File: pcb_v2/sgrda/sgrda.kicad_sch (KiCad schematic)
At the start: 17 parts, among them J1 addr_decoder, U1 74HC238, U2 74LS138, U3 74LS04

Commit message: arquivos no note
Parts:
- removed C3: 100nF, Capacitor_THT:C_Disc_D4.7mm_W2.5mm_P5.00mm, symbol Device:C
- removed unit 7 of U3
- removed unit 2 of U3
- removed unit 6 of U3
- added C4: 100nF, Capacitor_THT:C_Disc_D4.7mm_W2.5mm_P5.00mm, symbol Device:C
- added unit 7 of U4
- added unit 3 of U4
- added unit 1 of U4
- renumbered U3 to U4
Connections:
- net +5V: now also C4.1, U4.14 (VCC)
- net GND: now also C4.2, U4.7 (GND)
- net read_zero: now also U4.4; no longer U4.10
- net wr_addr_3: now also U1.4 (~{E1}); no longer U1.6 (E3)
- net write_clock: now also U1.6 (E3); no longer U1.4 (~{E1})
- net at U2.15 (O0): now also U4.3; no longer U4.11
- net enable_data_in renamed ~{enable_data_in}
- net enable_data_out renamed ~{enable_data_out}
- net n_read_A renamed ~{read_A}
- net n_read_B renamed ~{read_B}
- net n_read_C renamed ~{read_C}
- net n_read_D renamed ~{read_D}
- net n_read_E renamed ~{read_E}
- net n_read_H renamed ~{read_H}
- net n_read_L renamed ~{read_L}

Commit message: arquivos do gdrive
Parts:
- removed D1, D2, D3, D4, D5, D6: 1N4148, Diode_THT:D_DO-35_SOD27_P7.62mm_Horizontal, symbol Diode:1N4148
- removed R1, R2: 4.7K, Resistor_THT:R_Axial_DIN0207_L6.3mm_D2.5mm_P7.62mm_Horizontal, symbol Device:R
- added C3: 100nF, Capacitor_THT:C_Disc_D4.7mm_W2.5mm_P5.00mm, symbol Device:C
- added U3: 74LS32, Package_DIP:DIP-14_W7.62mm, symbol 74xx:74LS32
- D7: value LED -> POWER
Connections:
- net +5V: now also C3.1, U3.14 (VCC)
- net GND: now also U4.1, U4.11, U4.13, U4.5, U4.9, C3.2, U3.7 (GND)
- net rd_addr_3: now also U3.1
- net rd_addr_4: now also U3.2
- net read_zero: now also U3.4
- net wr_addr_3: now also U3.10
- net wr_addr_4: now also U3.9
- net write_zero: now also U3.12
- net ~{enable_data_in}: now also U3.11
- net ~{enable_data_out}: now also U3.6
- new net: U3.13, U3.8
- new net: U3.3, U3.5
- no-connect marks 23 -> 18

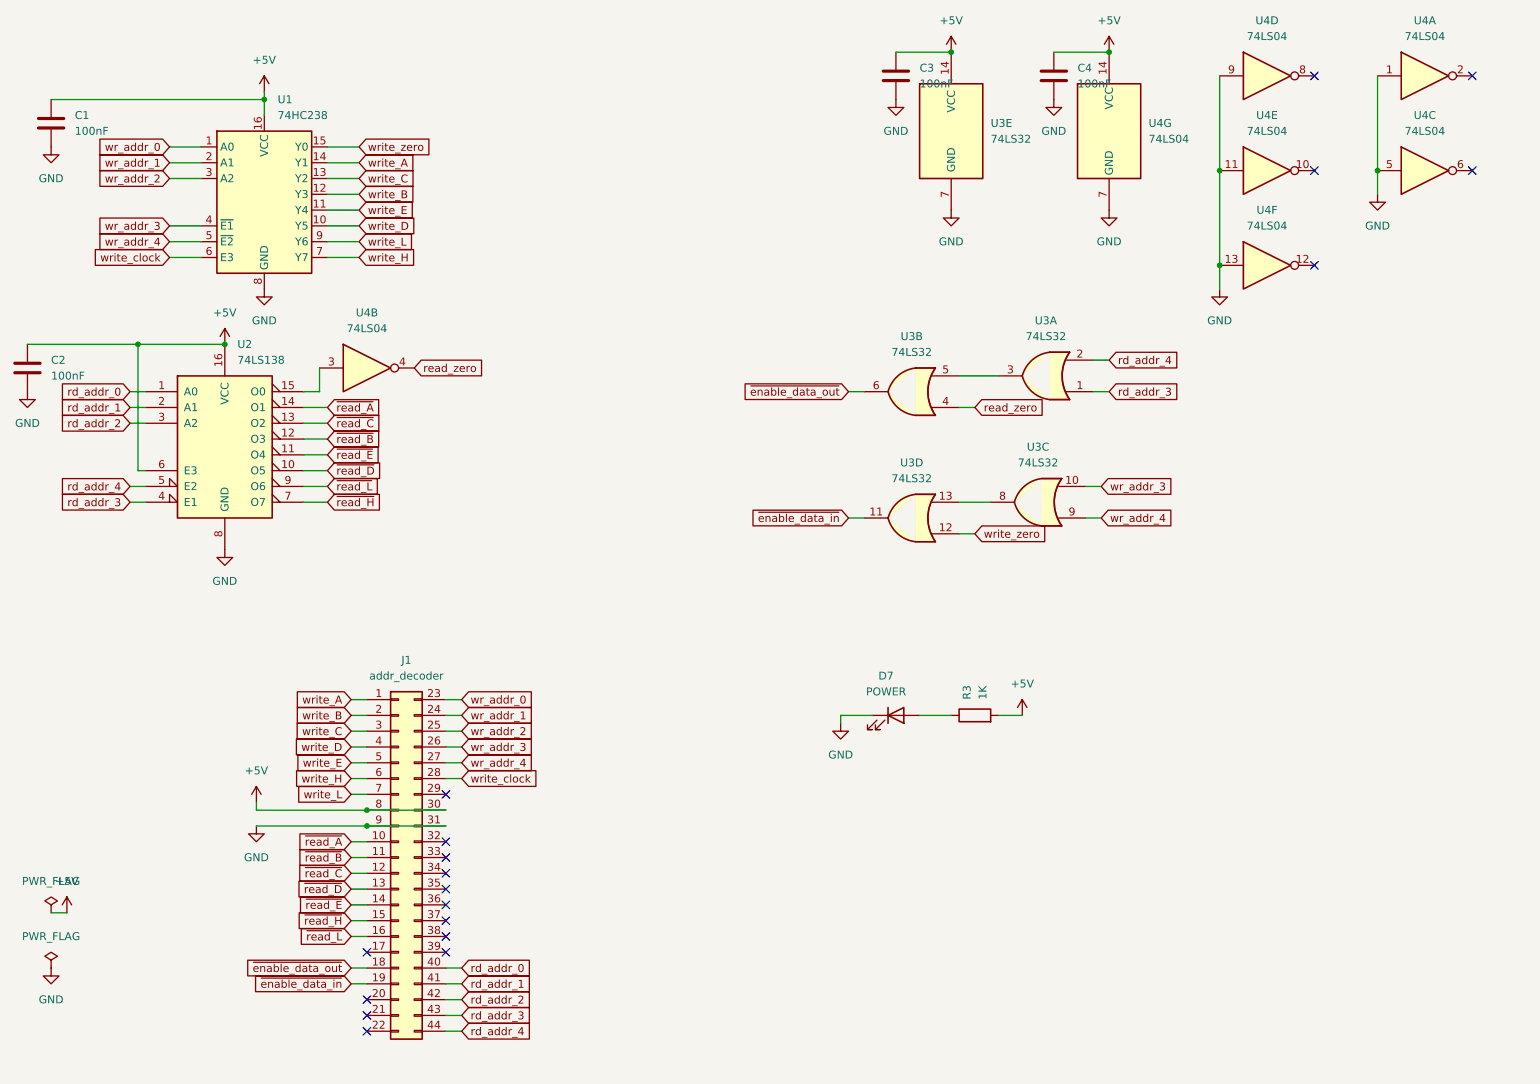
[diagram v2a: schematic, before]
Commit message: revisao completa; mgrfa agora inclui sr8 e sgrda; remover estes dois no proximo commit
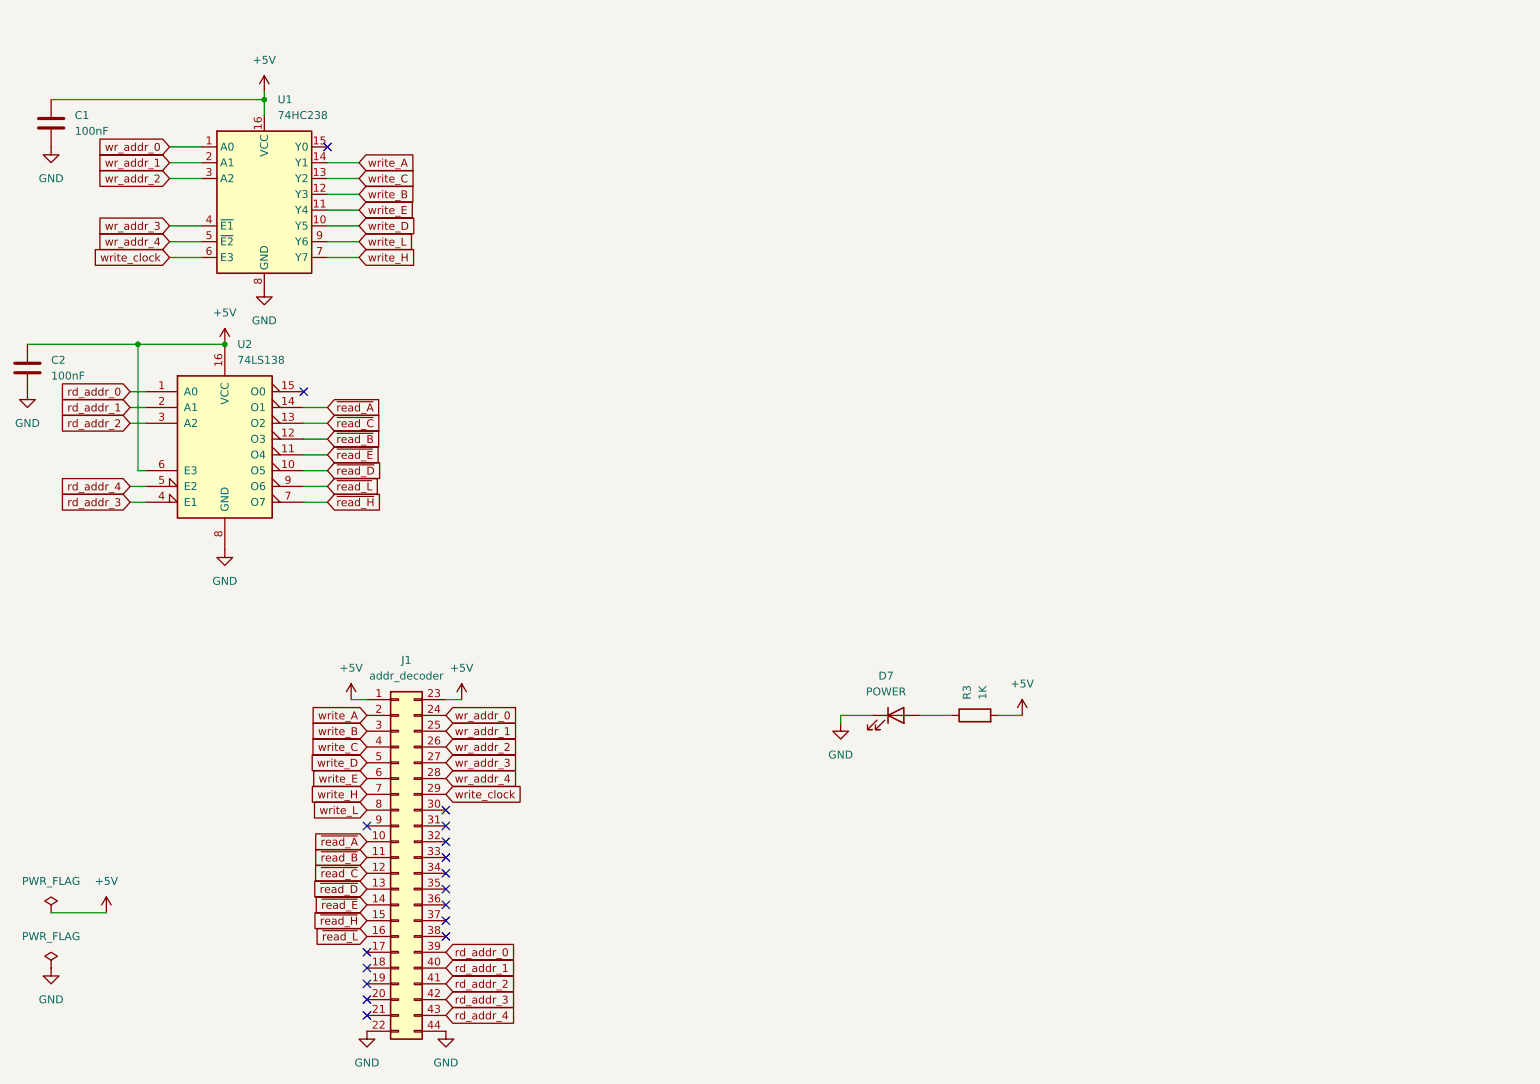
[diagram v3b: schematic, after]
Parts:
- removed C3, C4: 100nF, Capacitor_THT:C_Disc_D4.7mm_W2.5mm_P5.00mm, symbol Device:C
- removed U3: 74LS32, Package_DIP:DIP-14_W7.62mm, symbol 74xx:74LS32
- removed U4: 74LS04, Package_DIP:DIP-14_W7.62mm, symbol 74xx:74LS04
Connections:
- net +5V: now also J1.1 (Pin_1), J1.23 (Pin_23); no longer J1.30 (Pin_30), J1.8 (Pin_8)
- net GND: now also J1.22 (Pin_22), J1.44 (Pin_44); no longer J1.31 (Pin_31), J1.9 (Pin_9)
- net rd_addr_0: now also J1.39 (Pin_39); no longer J1.40 (Pin_40)
- net rd_addr_1: now also J1.40 (Pin_40); no longer J1.41 (Pin_41)
- net rd_addr_2: now also J1.41 (Pin_41); no longer J1.42 (Pin_42)
- net rd_addr_3: now also J1.42 (Pin_42); no longer J1.43 (Pin_43)
- net rd_addr_4: now also J1.43 (Pin_43); no longer J1.44 (Pin_44)
- net wr_addr_0: now also J1.24 (Pin_24); no longer J1.23 (Pin_23)
- net wr_addr_1: now also J1.25 (Pin_25); no longer J1.24 (Pin_24)
- net wr_addr_2: now also J1.26 (Pin_26); no longer J1.25 (Pin_25)
- net wr_addr_3: now also J1.27 (Pin_27); no longer J1.26 (Pin_26)
- net wr_addr_4: now also J1.28 (Pin_28); no longer J1.27 (Pin_27)
- net write_A: now also J1.2 (Pin_2); no longer J1.1 (Pin_1)
- net write_B: now also J1.3 (Pin_3); no longer J1.2 (Pin_2)
- net write_C: now also J1.4 (Pin_4); no longer J1.3 (Pin_3)
- net write_D: now also J1.5 (Pin_5); no longer J1.4 (Pin_4)
- net write_E: now also J1.6 (Pin_6); no longer J1.5 (Pin_5)
- net write_H: now also J1.7 (Pin_7); no longer J1.6 (Pin_6)
- net write_L: now also J1.8 (Pin_8); no longer J1.7 (Pin_7)
- net write_clock: now also J1.29 (Pin_29); no longer J1.28 (Pin_28)
- net write_zero: no longer names the net of U1.15 (Y0)
- net ~{enable_data_in}: no longer names the net of J1.19 (Pin_19)
- net ~{enable_data_out}: no longer names the net of J1.18 (Pin_18)
- no-connect marks 18 -> 17
